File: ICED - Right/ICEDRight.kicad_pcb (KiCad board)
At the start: 2 copper layers, 175.4 x 145 mm, 164 parts, among them P1 FLASH_HDR, P2 USBC, P3 CONN_17, P4 USB3_AFEMALE, Q1 TC1264, U1 MK20DX256VLH7, U2 IS31FL3731C, X1 CRYSTAL

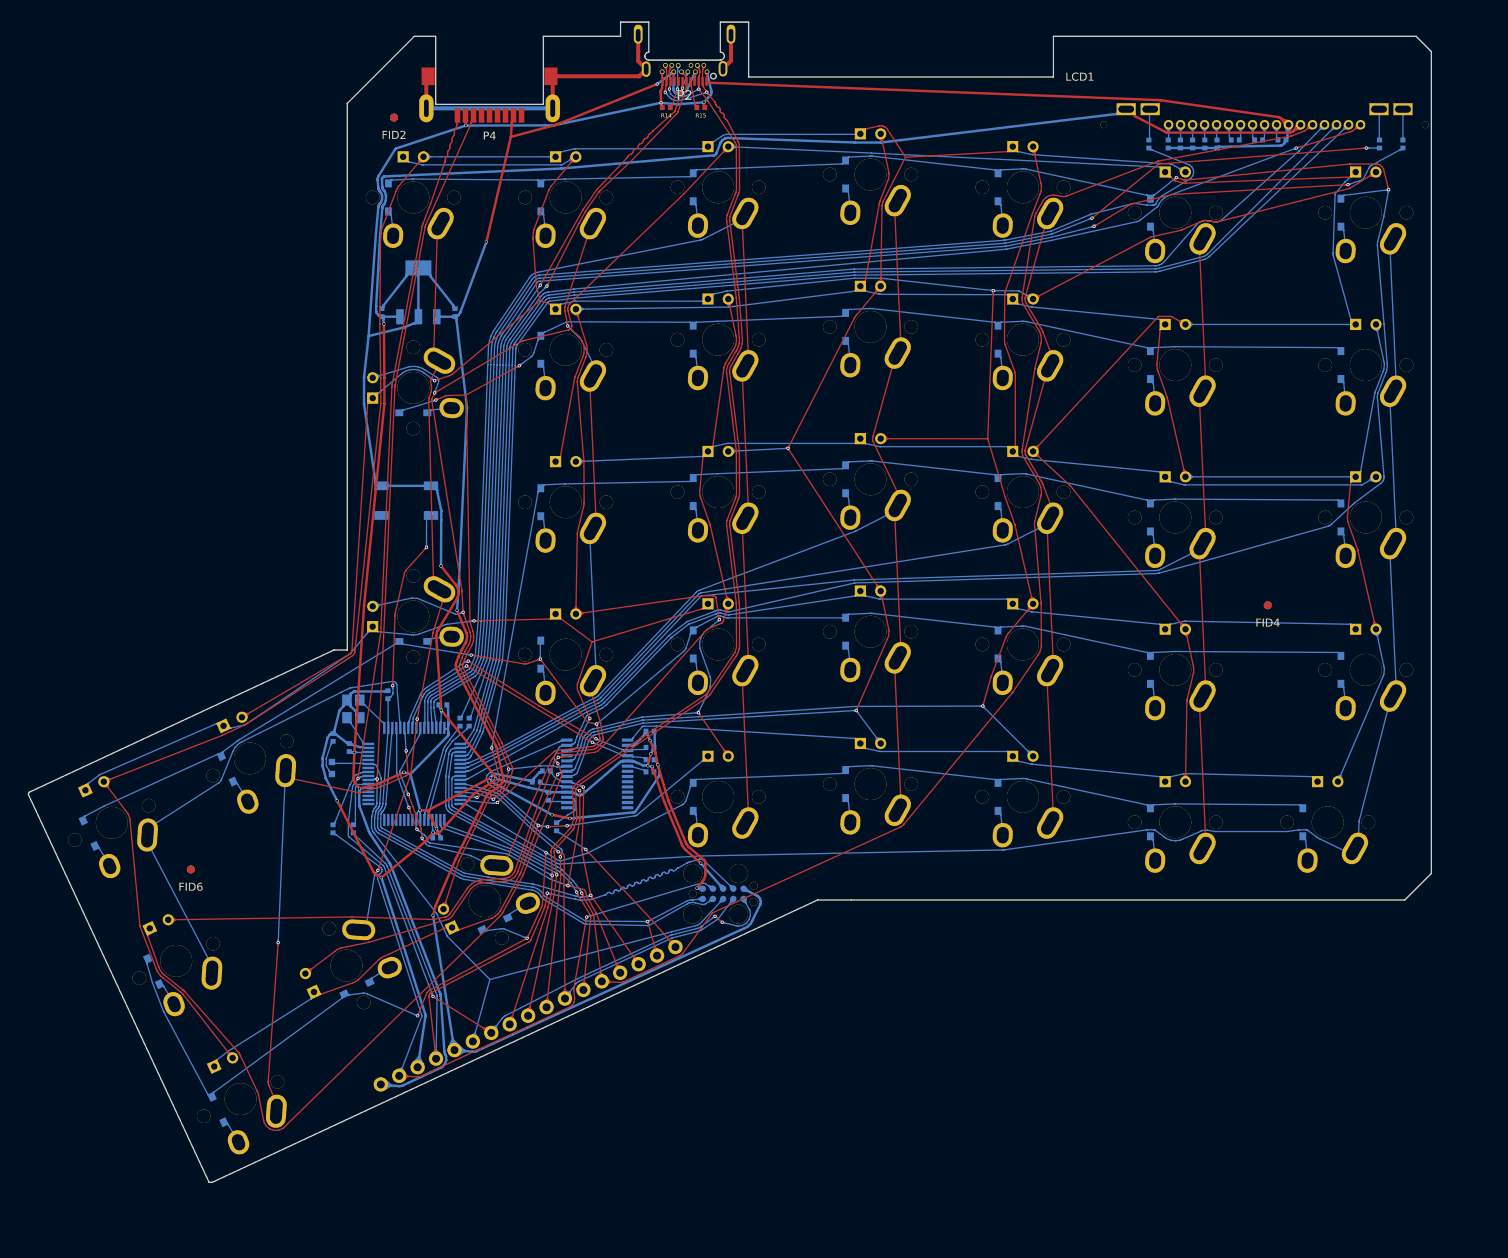
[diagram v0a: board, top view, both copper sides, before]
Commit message: Upgrade project + Right changes
- Replace MXALPS sockets by Kailh Hot-swaps
- Replace the LED controller
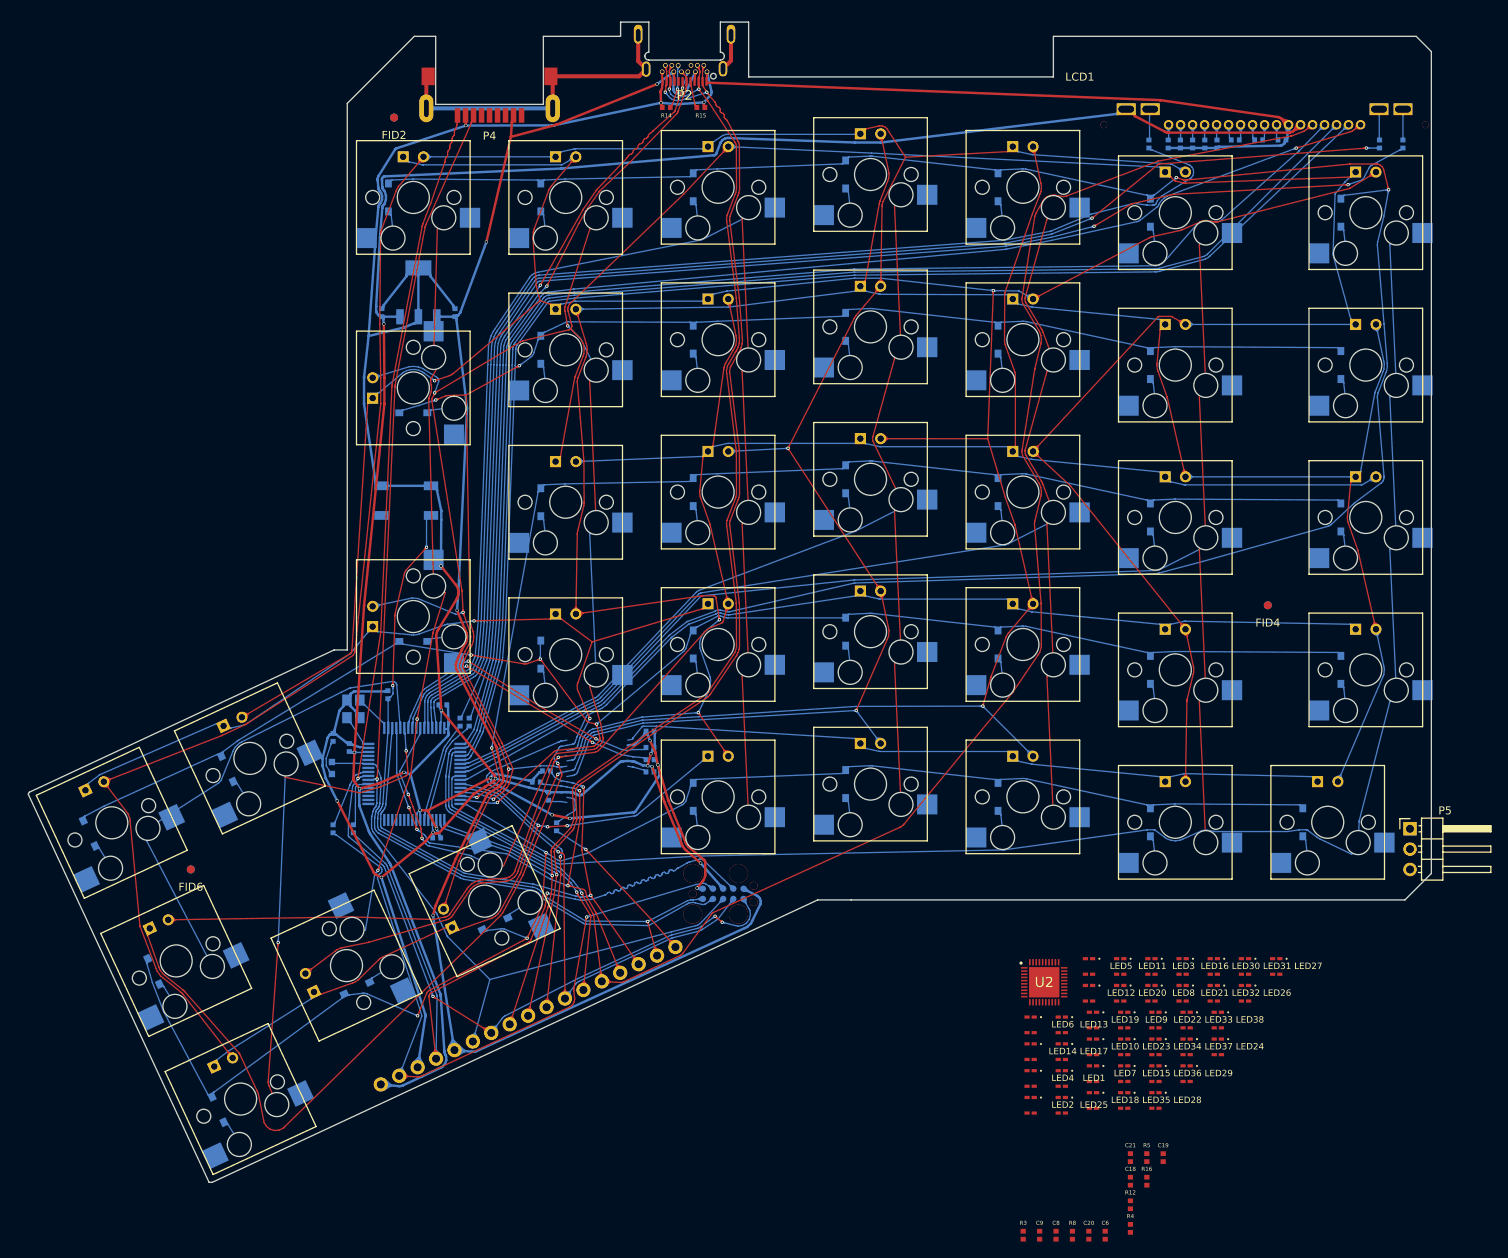
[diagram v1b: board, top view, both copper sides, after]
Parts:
- added C18: 0.1uF, prettylib:SMD-1005, F.Cu at (162.0, 188.1)
- added C19: 0.1uF, prettylib:SMD-1005, F.Cu at (166.1, 185.1)
- added C20: 0.1uF, prettylib:SMD-1005, F.Cu at (156.8, 194.8)
- added C21: 0.47uF, prettylib:SMD-1005, F.Cu at (162.0, 185.1)
- added C6: 0.47uF, prettylib:SMD-1005, F.Cu at (158.9, 194.8)
- added C8: 0.47uF, prettylib:SMD-1005, F.Cu at (152.7, 194.8)
- added C9: 0.47uF, prettylib:SMD-1005, F.Cu at (150.7, 194.8)
- added LED1: RGB_0606, prettylib:0606, F.Cu at (153.5, 175.2)
- added LED10: RGB_0606, prettylib:0606, F.Cu at (157.4, 171.3)
- added LED11: RGB_0606, prettylib:0606, F.Cu at (160.8, 161.2)
- added LED12: RGB_0606, prettylib:0606, F.Cu at (156.9, 164.6)
- added LED13: RGB_0606, prettylib:0606, F.Cu at (153.5, 168.5)
- added LED14: RGB_0606, prettylib:0606, F.Cu at (149.6, 171.9)
- added LED15: RGB_0606, prettylib:0606, F.Cu at (161.3, 174.6)
- added LED16: RGB_0606, prettylib:0606, F.Cu at (168.6, 161.2)
- added LED17: RGB_0606, prettylib:0606, F.Cu at (153.5, 171.9)
- added LED18: RGB_0606, prettylib:0606, F.Cu at (157.4, 178.0)
- added LED19: RGB_0606, prettylib:0606, F.Cu at (157.4, 167.9)
- added LED2: RGB_0606, prettylib:0606, F.Cu at (149.6, 178.6)
- added LED20: RGB_0606, prettylib:0606, F.Cu at (160.8, 164.6)
- added LED21: RGB_0606, prettylib:0606, F.Cu at (168.6, 164.6)
- added LED22: RGB_0606, prettylib:0606, F.Cu at (165.2, 167.9)
- added LED23: RGB_0606, prettylib:0606, F.Cu at (161.3, 171.3)
- added LED24: RGB_0606, prettylib:0606, F.Cu at (173.0, 171.3)
- added LED25: RGB_0606, prettylib:0606, F.Cu at (153.5, 178.6)
- added LED26: RGB_0606, prettylib:0606, F.Cu at (176.4, 164.6)
- added LED27: RGB_0606, prettylib:0606, F.Cu at (180.3, 161.2)
- added LED28: RGB_0606, prettylib:0606, F.Cu at (165.2, 178.0)
- added LED29: RGB_0606, prettylib:0606, F.Cu at (169.1, 174.6)
- added LED3: RGB_0606, prettylib:0606, F.Cu at (164.7, 161.2)
- added LED30: RGB_0606, prettylib:0606, F.Cu at (172.5, 161.2)
- added LED31: RGB_0606, prettylib:0606, F.Cu at (176.4, 161.2)
- added LED32: RGB_0606, prettylib:0606, F.Cu at (172.5, 164.6)
- added LED33: RGB_0606, prettylib:0606, F.Cu at (169.1, 167.9)
- added LED34: RGB_0606, prettylib:0606, F.Cu at (165.2, 171.3)
- added LED35: RGB_0606, prettylib:0606, F.Cu at (161.3, 178.0)
- added LED36: RGB_0606, prettylib:0606, F.Cu at (165.2, 174.6)
- added LED37: RGB_0606, prettylib:0606, F.Cu at (169.1, 171.3)
- added LED38: RGB_0606, prettylib:0606, F.Cu at (173.0, 167.9)
- added LED4: RGB_0606, prettylib:0606, F.Cu at (149.6, 175.2)
- added LED5: RGB_0606, prettylib:0606, F.Cu at (156.9, 161.2)
- added LED6: RGB_0606, prettylib:0606, F.Cu at (149.6, 168.5)
- added LED7: RGB_0606, prettylib:0606, F.Cu at (157.4, 174.6)
- added LED8: RGB_0606, prettylib:0606, F.Cu at (164.7, 164.6)
- added LED9: RGB_0606, prettylib:0606, F.Cu at (161.3, 167.9)
- added P5: RGB Out, Connector_PinHeader_2.54mm:PinHeader_1x03_P2.54mm_Horizontal, F.Cu at (197.0, 144.0)
- added R12: 20k, prettylib:SMD-1005, F.Cu at (162.0, 191.0)
- added R16: 4.7, prettylib:SMD-1005, F.Cu at (164.1, 188.1)
- added R3: 4.7, prettylib:SMD-1005, F.Cu at (148.6, 194.8)
- added R4: 100k, prettylib:SMD-1005, F.Cu at (162.0, 194.0)
- added R5: 4.7, prettylib:SMD-1005, F.Cu at (164.1, 185.1)
- added R8: 100k, prettylib:SMD-1005, F.Cu at (154.8, 194.8)
- S1, S10, S11, S12, S13, S14, S15, S16, S17, S18, S19, S2, S20, S21, S22, S23, S24, S25, S26, S27, S28, S29, S3, S30, S31, S32, S33, S34, S35, S36, S37, S38, S4, S5, S6, S7, S8, S9: footprint prettylib:MXALPS -> prettylib:SW_Hotswap_Kailh
- U2: value IS31FL3731C -> IS31FL3737-QFLS4-TR; footprint prettylib:SSOP-28 -> prettylib:QFN40P500X500X80-41N-D; moved to F.Cu
- moved U2 61.6 mm to (151.3, 163.2), turned to 0 degrees
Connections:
- P2 pad 20: Net-(P2-Pad20) -> unconnected-(P2-Pad20)
- P2 pad 8: Net-(P2-Pad8) -> unconnected-(P2-Pad8)
- P3 pad 14: /mcu/SDA0 -> /mcu/INTB
- P3 pad 15: /mcu/SCL0 -> /mcu/INTB
- P3 pad 17: /mcu/AUD -> /mcu/RGBOUT
- P4 pad 2: Net-(P4-Pad2) -> unconnected-(P4-Pad2)
- P4 pad 3: Net-(P4-Pad3) -> unconnected-(P4-Pad3)
- P4 pad 7: Net-(P4-Pad7) -> unconnected-(P4-Pad7)
- P4 pad 8: Net-(P4-Pad8) -> unconnected-(P4-Pad8)
- P4 pad 9: Net-(P4-Pad9) -> unconnected-(P4-Pad9)
- S39 pad 1: Net-(S39-Pad1) -> unconnected-(S39-Pad1)
- U1 pad 13: Net-(U1-Pad13) -> unconnected-(U1-Pad13)
- U1 pad 14: Net-(U1-Pad14) -> unconnected-(U1-Pad14)
- U1 pad 15: Net-(U1-Pad15) -> unconnected-(U1-Pad15)
- U1 pad 16: Net-(U1-Pad16) -> unconnected-(U1-Pad16)
- U1 pad 17: Net-(U1-Pad17) -> unconnected-(U1-Pad17)
- U1 pad 18: Net-(U1-Pad18) -> unconnected-(U1-Pad18)
- U1 pad 19: Net-(U1-Pad19) -> unconnected-(U1-Pad19)
- U1 pad 20: Net-(U1-Pad20) -> unconnected-(U1-Pad20)
- U1 pad 29: /mcu/PTA13 -> /mcu/RGBOUT
- U1 pad 35: /mcu/SCL0 -> /mcu/INTB
- U1 pad 36: /mcu/SDA0 -> /mcu/INTB
- U2 pad 1: /ledmatrix/CA9 -> /mcu/ledmatrix_2/Red1
- U2 pad 10: /mcu/CB4 -> /mcu/ledmatrix_2/Blue3
- U2 pad 11: /mcu/CB5 -> VSS
- U2 pad 12: /mcu/CB6 -> /mcu/ledmatrix_2/Red4
- U2 pad 13: /mcu/CB7 -> /mcu/ledmatrix_2/Green4
- U2 pad 14: /mcu/CB8 -> /mcu/ledmatrix_2/Blue4
- U2 pad 15: /mcu/CB9 -> /mcu/ledmatrix_2/Row1A
- U2 pad 16: Net-(C9-Pad1) -> /mcu/ledmatrix_2/Row1B
- U2 pad 17: Net-(C8-Pad1) -> /mcu/ledmatrix_2/Row2A
- U2 pad 18: VSS -> /mcu/ledmatrix_2/Row2B
- U2 pad 19: /mcu/SDA0 -> VDD
- U2 pad 2: VDD -> /mcu/ledmatrix_2/Green1
- U2 pad 20: /mcu/SCL0 -> /mcu/ledmatrix_2/Row3A
- U2 pad 21: /ledmatrix/CA1 -> /mcu/ledmatrix_2/Row3B
- U2 pad 22: /ledmatrix/CA2 -> /mcu/ledmatrix_2/Row4A
- U2 pad 23: /ledmatrix/CA3 -> /mcu/ledmatrix_2/Row4B
- U2 pad 24: /ledmatrix/CA4 -> /mcu/ledmatrix_2/Row4C
- U2 pad 25: /ledmatrix/CA5 -> /mcu/ledmatrix_2/Row5A
- U2 pad 26: /ledmatrix/CA6 -> VDD
- U2 pad 27: /ledmatrix/CA7 -> /mcu/ledmatrix_2/Row5B
- U2 pad 28: /ledmatrix/CA8 -> unconnected-(U2-Pad28)
- U2 pad 3: /mcu/SDB -> /mcu/ledmatrix_2/Blue1
- U2 pad 4: /mcu/INTB -> VSS
- U2 pad 5: VSS -> /mcu/ledmatrix_2/Red2
- U2 pad 6: Net-(R12-Pad1) -> /mcu/ledmatrix_2/Green2
- U2 pad 7: /mcu/CB1 -> /mcu/ledmatrix_2/Blue2
- U2 pad 8: /mcu/CB2 -> /mcu/ledmatrix_2/Red3
- U2 pad 9: /mcu/CB3 -> /mcu/ledmatrix_2/Green3
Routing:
- net /Row3: track 147.6 -> 316.2 mm
- net /mcu/RST: track 168.5 -> 0.00 mm
- net /Col7: track 162.5 -> 0.00 mm
- net /mcu/INTB: track 38.7 -> 152.1 mm, vias 2 -> 6
- net /mcu/MOSI: track 209.6 -> 289.1 mm
- net /mcu/TX1: track 165.5 -> 242.6 mm
- net /Col5: track 166.8 -> 89.7 mm
- net /Col8: track 178.9 -> 101.8 mm
- net /ledmatrix/CA2: track 421.7 -> 498.8 mm
- net /mcu/SCL0: track 73.9 -> 0.00 mm, vias 2 -> 0
- net /mcu/RX1: track 164.9 -> 236.0 mm, vias 3 -> 7
- net /mcu/SDA0: track 71.0 -> 0.00 mm, vias 4 -> 0
- net /Col4: track 118.4 -> 179.4 mm, vias 3 -> 2
- net /mcu/SDB: track 39.4 -> 0.00 mm, vias 2 -> 0
- net /mcu/RGBOUT: track 0.00 -> 23.6 mm, vias 0 -> 1
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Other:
- net class 4mil removed
- net class Default removed
- net class GND removed
- net class Power removed

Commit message: Place all LEDs with their switch + resistors
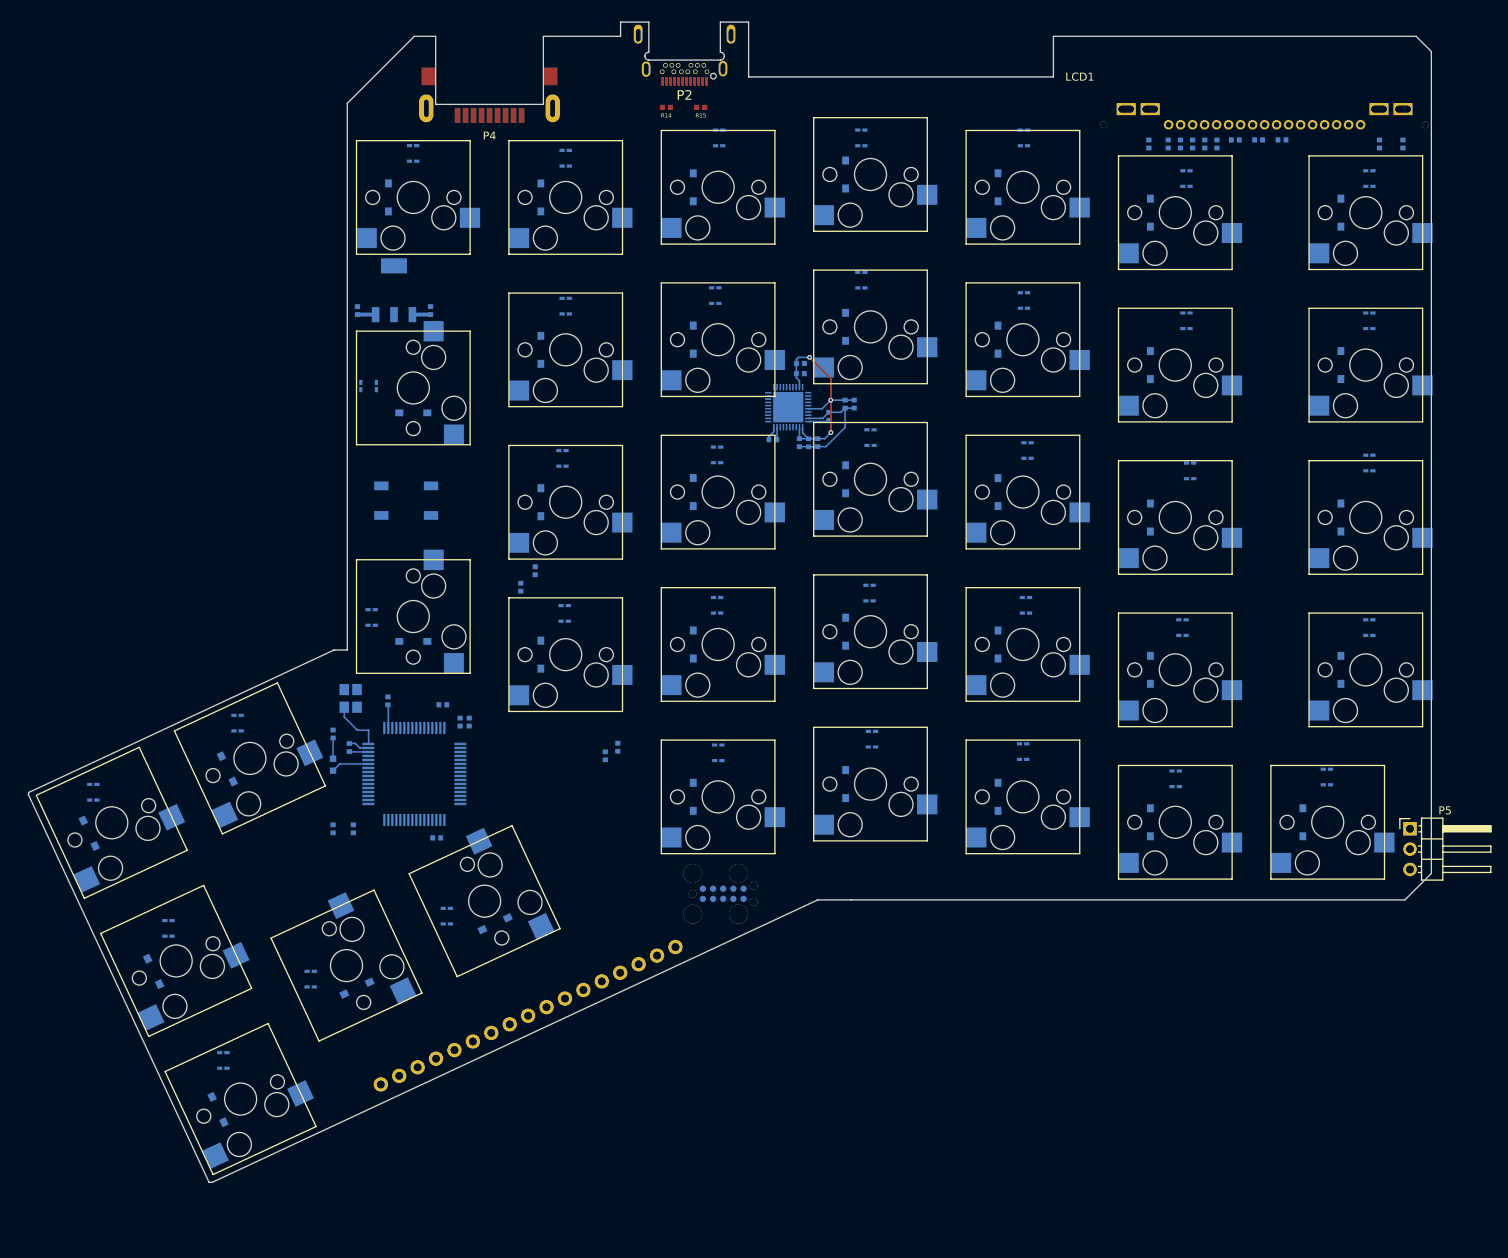
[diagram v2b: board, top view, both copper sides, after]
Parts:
- removed the C6 at (102.0, 131.8)
- removed the C8 at (90.3, 143.8)
- removed the C9 at (89.3, 140.0)
- removed D39, D40, D41, D42, D43, D44, D45, D46, D47, D48, D49, D50, D51, D52, D53, D54, D55, D56, D57, D58, D59, D60, D61, D62, D63, D64, D65, D66, D67, D68, D69, D70, D71, D72, D73, D74, D75, D76: LED, prettylib:INSW_LEDS_REG
- removed FID1, FID2, FID3, FID4, FID5, FID6: >VALUE, prettylib:FID
- removed IC_LOGO: , prettylib:IC_LOGO
- removed the R12 at (102.0, 136.9)
- removed the R3 at (102.0, 135.4)
- removed the R4 at (89.0, 136.8)
- removed the R5 at (87.8, 138.2)
- removed the R8 at (102.0, 133.9)
- C18, C19, C20, C21, C6, C8, C9, LED1, LED10, LED11, LED12, LED13, LED14, LED15, LED16, LED17, LED18, LED19, LED2, LED20, LED21, LED22, LED23, LED24, LED25, LED26, LED27, LED28, LED29, LED3, LED30, LED31, LED32, LED33, LED34, LED35, LED36, LED37, LED38, LED4, LED5, LED6, LED7, LED8, LED9, R12, R16, R3, R4, R5, R8, U2: moved to B.Cu
- moved LED1 141.2 mm to (72.4, 59.6)
- moved LED21 138.5 mm to (32.4, 139.4)
- moved LED2 131.9 mm to (91.4, 60.2)
- moved LED30 130.8 mm to (41.8, 156.5)
- moved LED31 128.3 mm to (48.6, 173.0)
- moved LED8 123.8 mm to (66.8, 88.7), turned to -90 degrees
- moved LED22 120.6 mm to (50.4, 130.8)
- moved LED4 119.5 mm to (128.4, 57.7)
- moved LED7 117.1 mm to (191.9, 62.7)
- moved LED3 116.8 mm to (110.6, 57.7)
- moved C6 114.2 mm to (120.8, 87.1), turned to 90 degrees
- moved LED9 113.3 mm to (91.4, 78.7)
- moved LED32 112.9 mm to (59.6, 162.8)
- moved R4 110.9 mm to (87.6, 111.8)
- moved C18 110.2 mm to (120.8, 85.9), turned to 90 degrees
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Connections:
- P3 pad 14: /mcu/INTB -> /mcu/SDA0
- P3 pad 15: /mcu/INTB -> /mcu/SCL0
- R3 pad 1: /mcu/INTB -> /mcu/SCL0
- R5 pad 1: /mcu/INTB -> /mcu/SDA0
- U1 pad 35: /mcu/INTB -> /mcu/SCL0
- U1 pad 36: /mcu/INTB -> /mcu/SDA0
- U2 pad 34: /mcu/INTB -> /mcu/SDA0
- U2 pad 35: /mcu/INTB -> /mcu/SCL0
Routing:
- net /ledmatrix/CA2: track 498.8 -> 0.00 mm, vias 4 -> 0
- net /ledmatrix/CA1: track 386.3 -> 0.00 mm, vias 2 -> 0
- net /ledmatrix/CA3: track 383.6 -> 0.00 mm, vias 3 -> 0
- net VSS: track 403.3 -> 19.8 mm, vias 13 -> 0
- net VDD: track 354.6 -> 33.9 mm, vias 12 -> 3
- net /Row3: track 316.2 -> 0.00 mm, vias 2 -> 0
- net /ledmatrix/CA4: track 311.9 -> 0.00 mm, vias 2 -> 0
- net /Row1: track 302.4 -> 0.00 mm, vias 2 -> 0
- net /mcu/MOSI: track 289.1 -> 0.00 mm, vias 1 -> 0
- net /ledmatrix/CA5: track 284.4 -> 0.00 mm, vias 1 -> 0
- net /mcu/TX1: track 242.6 -> 0.00 mm, vias 3 -> 0
- net /mcu/RX1: track 236.0 -> 0.00 mm, vias 7 -> 0
- net +5V: track 211.7 -> 2.28 mm, vias 4 -> 0
- net /mcu/SCLK: track 209.0 -> 0.00 mm, vias 1 -> 0
- net /Row4: track 205.7 -> 0.00 mm, vias 4 -> 0
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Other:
- rule pad_to_mask_clearance: 0.0508 -> 0
